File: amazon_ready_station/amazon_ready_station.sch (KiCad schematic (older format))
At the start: 19 parts, among them J1 ESP 32 Left VIN GND to VP EN, J2 IR_RECVR_GND_VCC_DAT, J3 BMP180 VIN GND SCL SDA, J4 SSD1306 SDA SCL GND VCC, J5 ESP32 Right 3V3 GND to D22 D23, J6 MISC VIN GND SCL SDA, Q1 2N2219, SW1 SW_Push, SW2 SW_DIP_x01

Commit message: hackathon pcb semi-final draft
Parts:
- added J7: BRKOUT_LEFT, Connector_PinSocket_2.54mm:PinSocket_1x15_P2.54mm_Vertical, symbol Connector:Conn_01x15_Female
- added J8: BRKOUT_RIGHT, Connector_PinSocket_2.54mm:PinSocket_1x15_P2.54mm_Vertical, symbol Connector:Conn_01x15_Female
- J2: value IR_RECVR_GND_VCC_DAT -> IR_RECVR_DAT_VCC_GND; footprint Connector_PinSocket_2.54mm:PinSocket_1x03_P2.54mm_Vertical -> Connector_PinSocket_2.54mm:PinSocket_1x03_P2.54mm_Horizontal
- J4: value SSD1306 SDA SCL GND VCC -> SSD1306 GND VCC SCL SDA
- TP1, TP2, TP3, TP4, TP5, TP6: footprint TestPoint:TestPoint_Pad_D2.0mm -> TestPoint:TestPoint_THTPad_D2.0mm_Drill1.0mm
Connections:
- net labels added: 5VGD, 5VIN
- wire segments 82 -> 113
- no-connect marks 19 -> 0

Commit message: update pcb and add time slider to virginia demo
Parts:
- removed SW2: SW_DIP_x01, Button_Switch_SMD:SW_DIP_SPSTx01_Slide_6.7x4.1mm_W6.73mm_P2.54mm_LowProfile_JPin, symbol Switch:SW_DIP_x01
- added SW_MOD1: SW_Push, Button_Switch_SMD:SW_Push_1P1T_NO_6x6mm_H9.5mm, symbol Switch:SW_Push
- added TP10: TestPoint, amazon_ready_station:pad_left, symbol Connector:TestPoint
- added TP7, TP8: TestPoint, TestPoint:TestPoint_THTPad_D2.0mm_Drill1.0mm, symbol Connector:TestPoint
- added TP9: TestPoint, amazon_ready_station:pad_right, symbol Connector:TestPoint
- J2: value IR_RECVR_DAT_VCC_GND -> IR_RECVR_GND_VIN_DAT
- renumbered SW1 to SW_INT1
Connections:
- wire segments 113 -> 114
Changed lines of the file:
@@
 Wire Wire Line
 	5700 3950 5100 3950
-Connection ~ 4900 4850
+Connection ~ 4800 4850
 Wire Wire Line
 	5700 4050 5350 4050
@@
 $EndComp
 $Comp
-L Switch:SW_Push SW1
+L Switch:SW_Push SW_INT1
 U 1 1 604FFFBF
 P 3000 5650
-F 0 "SW1" H 3046 5602 50  0000 R CNN
+F 0 "SW_INT1" H 3046 5602 50  0000 R CNN
 F 1 "SW_Push" H 3150 5500 50  0000 R CNN
 F 2 "Button_Switch_SMD:SW_Push_1P1T_NO_6x6mm_H9.5mm" H 3000 5850 50  0001 C CNN
@@
 	3500 5000 3500 5350
 Wire Wire Line
-	3500 5350 3300 5350
-Wire Wire Line
 	3650 5350 3500 5350
 Connection ~ 3500 5350
@@
 Connection ~ 4650 4850
 Wire Wire Line
-	4650 4850 4900 4850
+	4650 4850 4750 4850
 Wire Wire Line
 	2800 5650 2700 5650
@@
 Wire Wire Line
 	2500 5000 3500 5000
-$Comp
-L Switch:SW_DIP_x01 SW2
-U 1 1 604E07E7
-P 3000 5350
-F 0 "SW2" H 2700 5500 50  0000 L CNN
-F 1 "SW_DIP_x01" H 2900 5500 50  0000 L CNN
-F 2 "Button_Switch_SMD:SW_DIP_SPSTx01_Slide_6.7x4.1mm_W6.73mm_P2.54mm_LowProfile_JPin" H 3000 5350 50  0001 C CNN
-F 3 "~" H 3000 5350 50  0001 C CNN
-	1    3000 5350
-	1    0    0    -1
-$EndComp
 Wire Wire Line
 	2350 4350 2500 4350
-Connection ~ 4800 4750
 $Comp
 L Device:R R4
@@
 Wire Wire Line
 	4650 6400 3900 6400
-Wire Wire Line
-	5150 6400 4950 6400
 $Comp
 L Connector:Conn_01x03_Female J2
@@
 P 5450 5950
 F 0 "J2" H 5478 5976 50  0000 L CNN
-F 1 "IR_RECVR_DAT_VCC_GND" H 5478 5885 50  0000 L CNN
+F 1 "IR_RECVR_GND_VIN_DAT" H 5478 5885 50  0000 L CNN
 F 2 "Connector_PinSocket_2.54mm:PinSocket_1x03_P2.54mm_Horizontal" H 5450 5950 50  0001 C CNN
 F 3 "~" H 5450 5950 50  0001 C CNN
@@
 	1    0    0    -1
 $EndComp
-Connection ~ 4900 3950
+Connection ~ 4800 3950
 Wire Wire Line
 	5350 4050 5350 3450
@@
 Wire Wire Line
 	5550 4250 5700 4250
-Text Label 4900 3950 0    50   ~ 0
+Text Label 4800 3950 0    50   ~ 0
 3V3
 Wire Wire Line
-	4900 3950 4900 4850
+	4800 3950 4800 4850
 $Comp
 L Connector:Conn_01x15_Female J7
@@
 	4350 4850 4650 4850
 Wire Wire Line
-	4900 3350 4900 3950
+	4800 3350 4800 3950
 Wire Wire Line
 	5350 4050 5350 4750
-Wire Wire Line
-	5250 5850 5150 5850
-Wire Wire Line
-	5150 5850 5150 6400
-Wire Wire Line
-	4800 6050 5250 6050
-Wire Wire Line
-	4800 4750 4800 6050
-Wire Wire Line
-	4900 5950 5250 5950
-Wire Wire Line
-	5350 4750 5500 4750
 Wire Wire Line
 	5700 4750 5700 4850
 Connection ~ 5350 4750
 Wire Wire Line
-	4900 4850 4900 5950
-Wire Wire Line
-	4900 4850 5650 4850
+	4800 4850 5650 4850
 Wire Wire Line
 	5650 4850 5650 4950
@@
 Connection ~ 5100 3950
 Wire Wire Line
-	5100 3950 4900 3950
+	5100 3950 4800 3950
 Wire Wire Line
 	4650 4150 5150 4150
@@
 	5000 4250 5550 4250
 Connection ~ 4700 4750
-Wire Wire Line
-	4700 4750 4800 4750
-Wire Wire Line
-	4800 4750 5300 4750
 Wire Wire Line
 	5150 4150 5150 5050
@@
 $EndComp
 Wire Wire Line
-	4900 3350 4950 3350
+	4800 3350 4950 3350
 Wire Wire Line
 	4950 3350 5150 3350
@@
 $EndComp
 Connection ~ 5150 3350
-Wire Wire Line
-	5150 3350 5350 3350
-$Comp
-L Connector:TestPoint TP4
-U 1 1 60762358
-P 5350 3350
-F 0 "TP4" H 5300 3550 50  0000 L CNN
-F 1 "TestPoint" V 5250 3350 50  0000 L CNN
-F 2 "TestPoint:TestPoint_THTPad_D2.0mm_Drill1.0mm" H 5550 3350 50  0001 C CNN
-F 3 "~" H 5550 3350 50  0001 C CNN
-	1    5350 3350
-	1    0    0    -1
-$EndComp
-Connection ~ 5350 3350
-Wire Wire Line
-	5350 3350 5750 3350
-$Comp
-L Connector:TestPoint TP5
-U 1 1 607625BD
-P 5500 4750
-F 0 "TP5" H 5450 4950 50  0000 L CNN
-F 1 "TestPoint" V 5400 4750 50  0000 L CNN
-F 2 "TestPoint:TestPoint_THTPad_D2.0mm_Drill1.0mm" H 5700 4750 50  0001 C CNN
-F 3 "~" H 5700 4750 50  0001 C CNN
-	1    5500 4750
-	1    0    0    -1
-$EndComp
-Connection ~ 5500 4750
-Wire Wire Line
-	5500 4750 5700 4750
 $Comp
 L Connector:TestPoint TP3
@@
 $EndComp
 Connection ~ 5700 4750
-Text Label 2600 4750 0    50   ~ 0
+Text Label 2550 4850 0    50   ~ 0
 5VIN
-Text Label 2600 4850 0    50   ~ 0
+Text Label 2550 4750 0    50   ~ 0
 5VGD
+Connection ~ 2850 4850
+$Comp
+L Connector:TestPoint TP10
+U 1 1 605C250F
+P 2850 4850
+F 0 "TP10" H 2800 5050 50  0000 L CNN
+F 1 "TestPoint" V 2950 4850 50  0000 L CNN
+F 2 "amazon_ready_station:pad_left" H 3050 4850 50  0001 C CNN
+F 3 "~" H 3050 4850 50  0001 C CNN
+	1    2850 4850
+	0    1    1    0
+$EndComp
+$Comp
+L Connector:TestPoint TP9
+U 1 1 605C4012
+P 2850 4750
+F 0 "TP9" H 2700 4950 50  0000 L CNN
+F 1 "TestPoint" V 2850 4900 50  0000 L CNN
+F 2 "amazon_ready_station:pad_right" H 3050 4750 50  0001 C CNN
+F 3 "~" H 3050 4750 50  0001 C CNN
+	1    2850 4750
+	0    1    1    0
+$EndComp
+Connection ~ 2850 4750
+Wire Wire Line
+	2350 4750 1450 4650
+Connection ~ 2350 4750
+Wire Wire Line
+	2350 4850 1450 5000
+Connection ~ 2350 4850
+$Comp
+L Connector:TestPoint TP8
+U 1 1 605CDAFA
+P 1450 5000
+F 0 "TP8" H 1300 5200 50  0000 L CNN
+F 1 "TestPoint" V 1450 5150 50  0000 L CNN
+F 2 "TestPoint:TestPoint_THTPad_D2.0mm_Drill1.0mm" H 1650 5000 50  0001 C CNN
+F 3 "~" H 1650 5000 50  0001 C CNN
+	1    1450 5000
+	0    -1   -1   0
+$EndComp
+$Comp
+L Connector:TestPoint TP7
+U 1 1 605CE0C4
+P 1450 4650
+F 0 "TP7" H 1400 4850 50  0000 L CNN
+F 1 "TestPoint" V 1550 4650 50  0000 L CNN
+F 2 "TestPoint:TestPoint_THTPad_D2.0mm_Drill1.0mm" H 1650 4650 50  0001 C CNN
+F 3 "~" H 1650 4650 50  0001 C CNN
+	1    1450 4650
+	0    -1   -1   0
+$EndComp
+Wire Wire Line
+	4700 4750 4900 4750
+Wire Wire Line
+	4900 4750 4900 5850
+Wire Wire Line
+	4900 5850 5250 5850
+Connection ~ 4900 4750
+Wire Wire Line
+	4900 4750 5300 4750
+Wire Wire Line
+	4750 4850 4750 5950
+Wire Wire Line
+	4750 5950 5250 5950
+Connection ~ 4750 4850
+Wire Wire Line
+	4750 4850 4800 4850
+Wire Wire Line
+	5250 6050 5250 6400
+Wire Wire Line
+	4950 6400 5250 6400
+Wire Wire Line
+	5150 3350 5750 3350
+Wire Wire Line
+	5350 4750 5700 4750
+$Comp
+L Switch:SW_Push SW_MOD1
+U 1 1 6063A1F9
+P 3000 5350
+F 0 "SW_MOD1" H 3046 5302 50  0000 R CNN
+F 1 "SW_Push" H 3150 5200 50  0000 R CNN
+F 2 "Button_Switch_SMD:SW_Push_1P1T_NO_6x6mm_H9.5mm" H 3000 5550 50  0001 C CNN
+F 3 "~" H 3000 5550 50  0001 C CNN
+	1    3000 5350
+	1    0    0    -1
+$EndComp
+Wire Wire Line
+	3200 5350 3500 5350
+Wire Wire Line
+	2800 5350 2700 5350
+$Comp
+L Connector:TestPoint TP5
+U 1 1 60657975
+P 1450 5000
+F 0 "TP5" H 1300 5200 50  0000 L CNN
+F 1 "TestPoint" V 1450 5150 50  0000 L CNN
+F 2 "TestPoint:TestPoint_THTPad_D2.0mm_Drill1.0mm" H 1650 5000 50  0001 C CNN
+F 3 "~" H 1650 5000 50  0001 C CNN
+	1    1450 5000
+	-1   0    0    1
+$EndComp
+Connection ~ 1450 5000
+$Comp
+L Connector:TestPoint TP4
+U 1 1 60658198
+P 1450 4650
+F 0 "TP4" H 1300 4850 50  0000 L CNN
+F 1 "TestPoint" V 1450 4800 50  0000 L CNN
+F 2 "TestPoint:TestPoint_THTPad_D2.0mm_Drill1.0mm" H 1650 4650 50  0001 C CNN
+F 3 "~" H 1650 4650 50  0001 C CNN
+	1    1450 4650
+	1    0    0    -1
+$EndComp
+Connection ~ 1450 4650
 $EndSCHEMATC

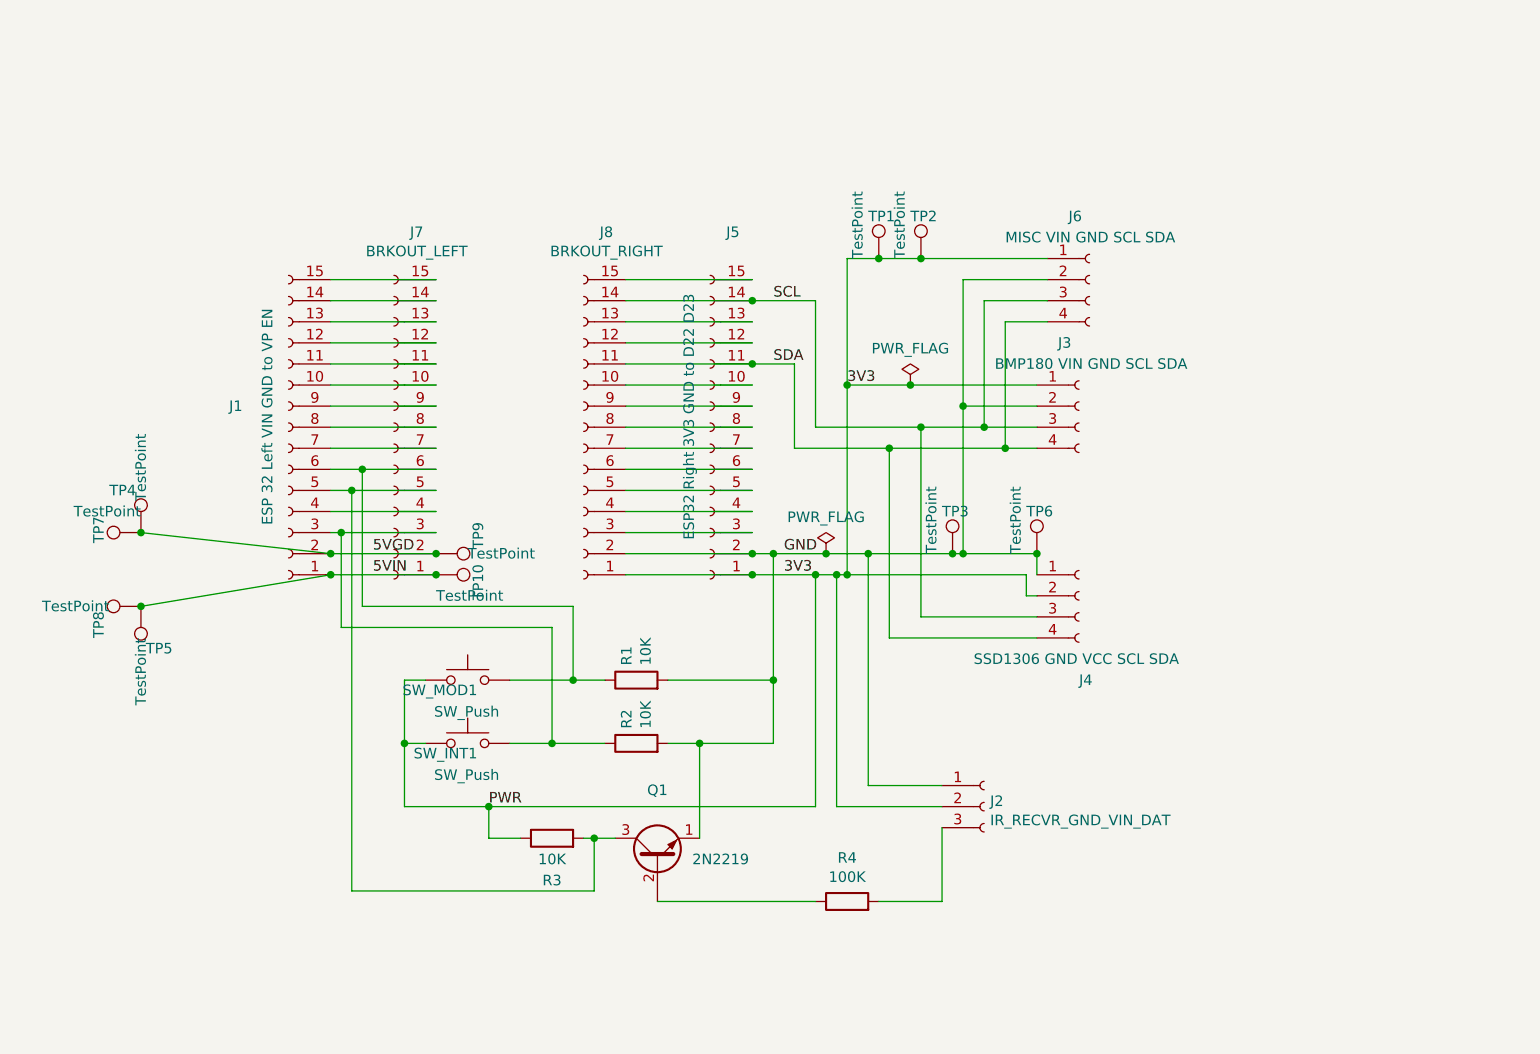
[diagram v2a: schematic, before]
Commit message: added artwork, edited silkscreen
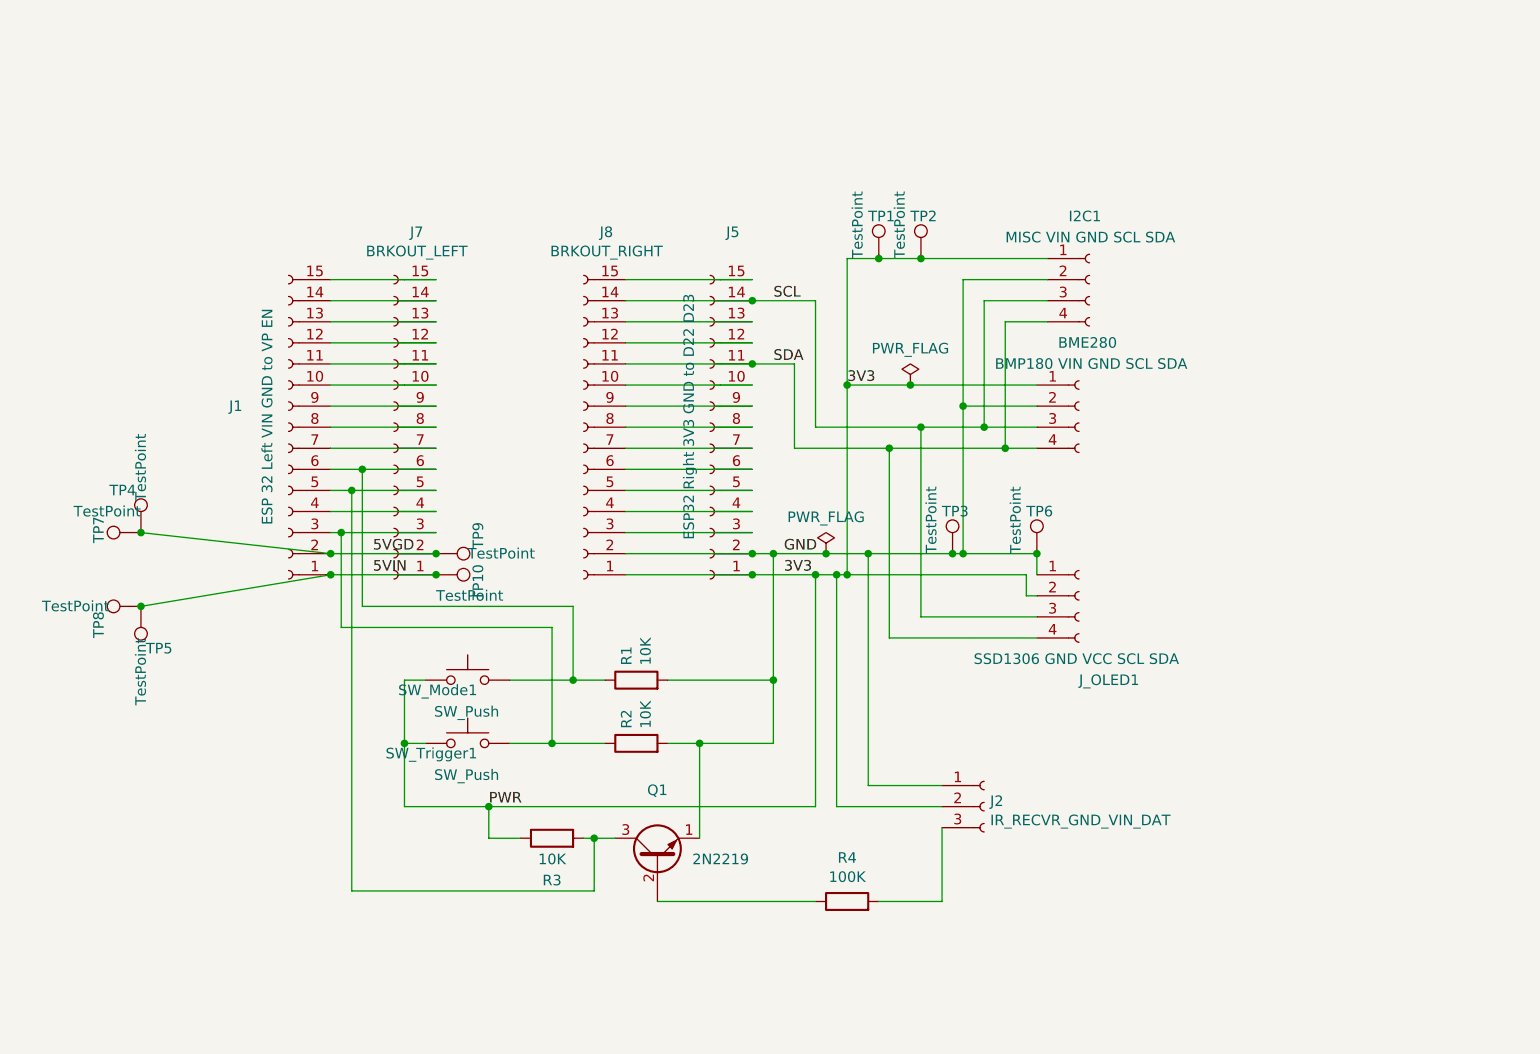
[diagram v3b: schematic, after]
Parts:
- renumbered J3 to BME280, J6 to I2C1, J4 to J_OLED1, SW_MOD1 to SW_Mode1, SW_INT1 to SW_Trigger1
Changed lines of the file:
@@
 	4350 3550 4650 3550
 $Comp
-L Connector:Conn_01x04_Female J3
+L Connector:Conn_01x04_Female BME280
 U 1 1 604E2AAF
 P 5900 4050
-F 0 "J3" H 5800 4350 50  0000 L CNN
+F 0 "BME280" H 5800 4350 50  0000 L CNN
 F 1 "BMP180 VIN GND SCL SDA" H 5500 4250 50  0000 L CNN
 F 2 "Connector_PinSocket_2.54mm:PinSocket_1x04_P2.54mm_Vertical" H 5900 4050 50  0001 C CNN
@@
 $EndComp
 $Comp
-L Connector:Conn_01x04_Female J4
+L Connector:Conn_01x04_Female J_OLED1
 U 1 1 604E4BCE
 P 5900 4950
-F 0 "J4" H 5900 4550 50  0000 L CNN
+F 0 "J_OLED1" H 5900 4550 50  0000 L CNN
 F 1 "SSD1306 GND VCC SCL SDA" H 5400 4650 50  0000 L CNN
 F 2 "Connector_PinSocket_2.54mm:PinSocket_1x04_P2.54mm_Vertical" H 5900 4950 50  0001 C CNN
@@
 $EndComp
 $Comp
-L Switch:SW_Push SW_INT1
+L Switch:SW_Push SW_Trigger1
 U 1 1 604FFFBF
 P 3000 5650
-F 0 "SW_INT1" H 3046 5602 50  0000 R CNN
+F 0 "SW_Trigger1" H 3046 5602 50  0000 R CNN
 F 1 "SW_Push" H 3150 5500 50  0000 R CNN
 F 2 "Button_Switch_SMD:SW_Push_1P1T_NO_6x6mm_H9.5mm" H 3000 5850 50  0001 C CNN
@@
 $EndComp
 $Comp
-L Connector:Conn_01x04_Female J6
+L Connector:Conn_01x04_Female I2C1
 U 1 1 605AD1B2
 P 5950 3450
-F 0 "J6" H 5850 3750 50  0000 L CNN
+F 0 "I2C1" H 5850 3750 50  0000 L CNN
 F 1 "MISC VIN GND SCL SDA" H 5550 3650 50  0000 L CNN
 F 2 "Connector_PinSocket_2.54mm:PinSocket_1x04_P2.54mm_Vertical" H 5950 3450 50  0001 C CNN
@@
 	5350 4750 5700 4750
 $Comp
-L Switch:SW_Push SW_MOD1
+L Switch:SW_Push SW_Mode1
 U 1 1 6063A1F9
 P 3000 5350
-F 0 "SW_MOD1" H 3046 5302 50  0000 R CNN
+F 0 "SW_Mode1" H 3046 5302 50  0000 R CNN
 F 1 "SW_Push" H 3150 5200 50  0000 R CNN
 F 2 "Button_Switch_SMD:SW_Push_1P1T_NO_6x6mm_H9.5mm" H 3000 5550 50  0001 C CNN
